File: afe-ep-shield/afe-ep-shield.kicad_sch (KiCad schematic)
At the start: 15 parts, among them J1 Conn_02x06_Odd_Even, J2 Conn_02x06_Odd_Even, J3 Conn_02x12_Odd_Even, J4 Conn_02x12_Odd_Even, J5 Conn_02x20_Odd_Even, U1 Dual_Buffer, U2 Dual_Buffer

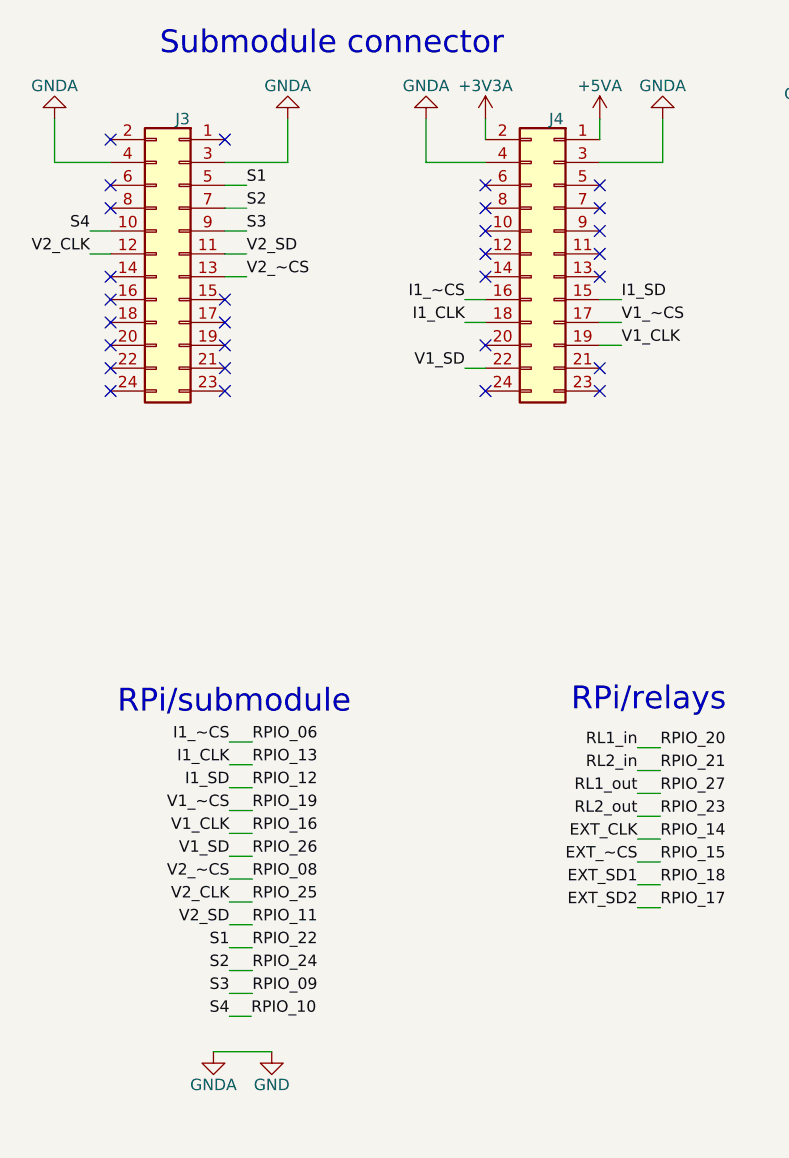
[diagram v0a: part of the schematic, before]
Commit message: Fixed afe shield connector
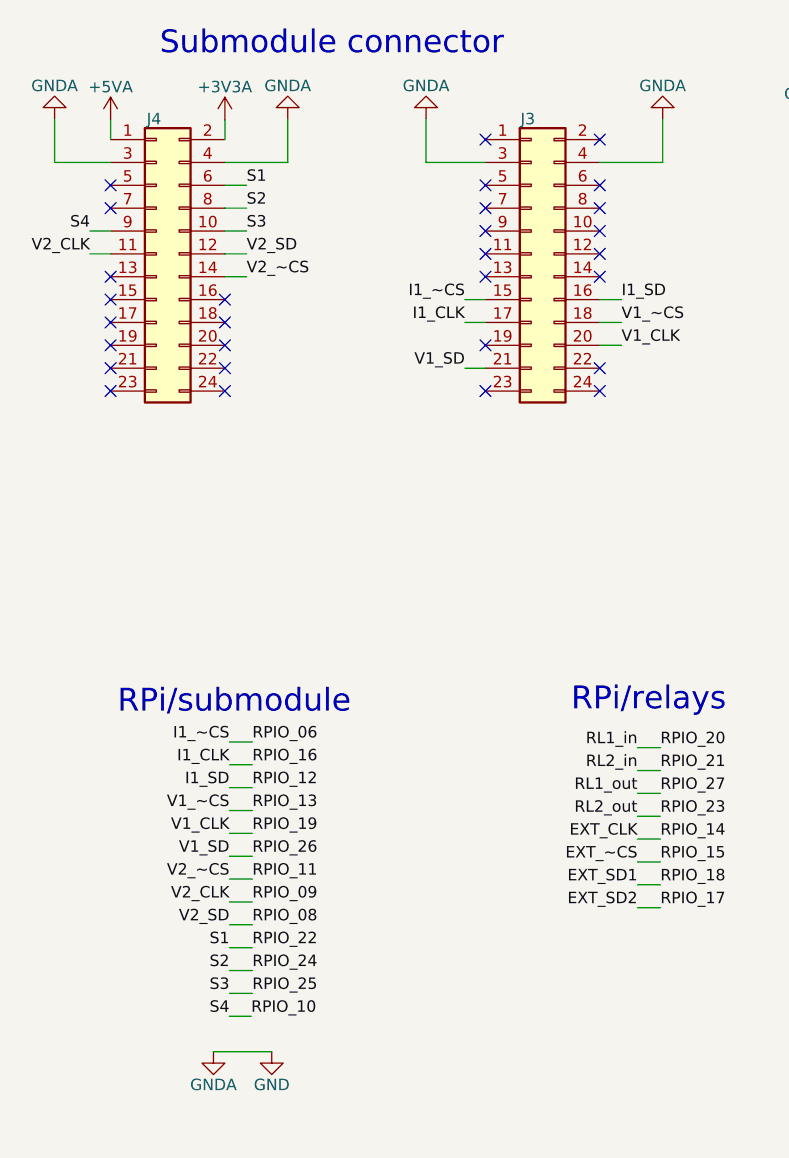
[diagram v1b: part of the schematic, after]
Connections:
- net I1_CLK: now also J3.17 (Pin_17), J5.36 (Pin_36); no longer J4.18 (Pin_18), J5.33 (Pin_33)
- net I1_SD: now also J3.16 (Pin_16); no longer J4.15 (Pin_15)
- net I1_~CS: now also J3.15 (Pin_15); no longer J4.16 (Pin_16)
- net RPIO_08: now also J4.12 (Pin_12); no longer J3.13 (Pin_13)
- net RPIO_09: now also J4.11 (Pin_11); no longer J3.9 (Pin_9)
- net RPIO_10: now also J4.9 (Pin_9); no longer J3.10 (Pin_10)
- net RPIO_11: now also J4.14 (Pin_14); no longer J3.11 (Pin_11)
- net RPIO_19: now also J3.20 (Pin_20); no longer J4.17 (Pin_17)
- net RPIO_22: now also J4.6 (Pin_6); no longer J3.5 (Pin_5)
- net RPIO_24: now also J4.8 (Pin_8); no longer J3.7 (Pin_7)
- net RPIO_25: now also J4.10 (Pin_10); no longer J3.12 (Pin_12)
- net RPIO_26: now also J3.21 (Pin_21); no longer J4.22 (Pin_22)
- net RPIO_13: now reaches J3.18 (Pin_18)
- net RPIO_13: now also J5.33 (Pin_33)
- net RPIO_16: no longer names the net of J4.19 (Pin_19)
- net RPIO_16: no longer J5.36 (Pin_36)
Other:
- moved on the sheet: J3, J4

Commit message: Connected 3V3A and 3V3 in afe shield
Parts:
- added R3: 0R, Resistor_SMD:R_0805_2012Metric, symbol Device:R_Small
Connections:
- net +3V3: now also J5.17 (Pin_17), R3.1; no longer J5.1 (Pin_1)
- net +3V3A: now also J3.2 (Pin_2), R3.2; no longer J4.2 (Pin_2)
- net GND: no longer J5.17 (Pin_17)
- no-connect marks 38 -> 39
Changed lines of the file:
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@@
   (junction (at 192.024 33.147) (diameter 0) (color 0 0 0 0)
-  )
-  (junction (at 98.552 48.768) (diameter 0) (color 0 0 0 0)
   )
   (junction (at 192.024 30.607) (diameter 0) (color 0 0 0 0)
@@
   (no_connect (at 170.307 30.607))
   (no_connect (at 63.373 27.559))
-  (no_connect (at 76.073 27.559))
+  (no_connect (at 34.417 27.559))
   (no_connect (at 109.601 30.988))
+  (no_connect (at 109.601 28.448))
   (no_connect (at 34.417 47.879))
   (no_connect (at 34.417 50.419))
@@
     (stroke (width 0) (type default) (color 0 0 0 0))
   )
+  (wire (pts (xy 57.785 62.23) (xy 57.785 64.77))
+    (stroke (width 0) (type default) (color 0 0 0 0))
+  )
   (wire (pts (xy 34.417 40.259) (xy 36.83 40.259))
     (stroke (width 0) (type default) (color 0 0 0 0))
@@
     (stroke (width 0) (type default) (color 0 0 0 0))
   )
+  (wire (pts (xy 50.165 64.77) (xy 47.625 64.77))
+    (stroke (width 0) (type default) (color 0 0 0 0))
+  )
   (wire (pts (xy 122.301 56.388) (xy 124.841 56.388))
     (stroke (width 0) (type default) (color 0 0 0 0))
@@
     (stroke (width 0) (type default) (color 0 0 0 0))
   )
-  (wire (pts (xy 34.417 25.4) (xy 34.417 27.559))
-    (stroke (width 0) (type default) (color 0 0 0 0))
-  )
   (wire (pts (xy 258.191 150.749) (xy 260.985 150.749))
     (stroke (width 0) (type default) (color 0 0 0 0))
@@
     (stroke (width 0) (type default) (color 0 0 0 0))
   )
-  (wire (pts (xy 98.552 48.768) (xy 109.601 48.768))
-    (stroke (width 0) (type default) (color 0 0 0 0))
-  )
   (wire (pts (xy 34.925 109.728) (xy 37.465 109.728))
     (stroke (width 0) (type default) (color 0 0 0 0))
@@
     (stroke (width 0) (type default) (color 0 0 0 0))
   )
-  (wire (pts (xy 98.552 48.768) (xy 98.552 38.608))
-    (stroke (width 0) (type default) (color 0 0 0 0))
-  )
   (wire (pts (xy 80.264 97.663) (xy 82.804 97.663))
     (stroke (width 0) (type default) (color 0 0 0 0))
@@
     (stroke (width 0) (type default) (color 0 0 0 0))
   )
+  (wire (pts (xy 93.472 48.768) (xy 109.601 48.768))
+    (stroke (width 0) (type default) (color 0 0 0 0))
+  )
   (wire (pts (xy 19.304 167.64) (xy 19.304 170.18))
     (stroke (width 0) (type default) (color 0 0 0 0))
@@
     (stroke (width 0) (type default) (color 0 0 0 0))
   )
-  (wire (pts (xy 98.552 48.768) (xy 98.552 58.928))
+  (wire (pts (xy 98.552 38.608) (xy 98.552 58.928))
     (stroke (width 0) (type default) (color 0 0 0 0))
   )
@@
     (stroke (width 0) (type default) (color 0 0 0 0))
   )
-  (wire (pts (xy 109.601 26.162) (xy 109.601 28.448))
-    (stroke (width 0) (type default) (color 0 0 0 0))
-  )
   (wire (pts (xy 34.925 119.888) (xy 37.465 119.888))
     (stroke (width 0) (type default) (color 0 0 0 0))
@@
     (stroke (width 0) (type default) (color 0 0 0 0))
   )
+  (wire (pts (xy 93.472 26.162) (xy 93.472 48.768))
+    (stroke (width 0) (type default) (color 0 0 0 0))
+  )
   (wire (pts (xy 122.301 28.448) (xy 122.301 30.988))
     (stroke (width 0) (type default) (color 0 0 0 0))
@@
     (stroke (width 0) (type default) (color 0 0 0 0))
   )
+  (wire (pts (xy 47.625 64.77) (xy 47.625 62.23))
+    (stroke (width 0) (type default) (color 0 0 0 0))
+  )
   (wire (pts (xy 172.212 55.499) (xy 172.212 52.959))
     (stroke (width 0) (type default) (color 0 0 0 0))
   )
+  (wire (pts (xy 76.073 25.273) (xy 76.073 27.559))
+    (stroke (width 0) (type default) (color 0 0 0 0))
+  )
   (wire (pts (xy 34.417 42.799) (xy 36.83 42.799))
+    (stroke (width 0) (type default) (color 0 0 0 0))
+  )
+  (wire (pts (xy 55.245 64.77) (xy 57.785 64.77))
     (stroke (width 0) (type default) (color 0 0 0 0))
   )
@@
     (pin "1")
   )
+  (symbol (lib_id "Device:R_Small") (at 52.705 64.77 270) (mirror x) (unit 1)
+    (in_bom yes) (on_board yes)
+    (property "Reference" "R3" (id 0) (at 51.435 68.326 90)
+      (effects (font (size 1.27 1.27)) (justify left))
+    )
+    (property "Value" "0R" (id 1) (at 51.435 66.548 90)
+      (effects (font (size 1.27 1.27)) (justify left))
+    )
+    (property "Footprint" "Resistor_SMD:R_0805_2012Metric" (id 2) (at 52.705 64.77 0)
+      (effects (font (size 1.27 1.27)) hide)
+    )
+    (property "Datasheet" "~" (id 3) (at 52.705 64.77 0)
+      (effects (font (size 1.27 1.27)) hide)
+    )
+    (pin "1")
+    (pin "2")
+  )
   (symbol (lib_id "power:VCC") (at 205.359 52.959 0) (unit 1)
     (in_bom yes) (on_board yes)
@@
     )
     (property "Datasheet" "" (id 3) (at 205.359 52.959 0)
+      (effects (font (size 1.27 1.27)) hide)
+    )
+    (pin "1")
+  )
+  (symbol (lib_id "CL_power:+3V3A") (at 47.625 62.23 0) (unit 1)
+    (in_bom yes) (on_board yes)
+    (property "Reference" "#PWR06" (id 0) (at 47.625 66.04 0)
+      (effects (font (size 1.27 1.27)) hide)
+    )
+    (property "Value" "+3V3A" (id 1) (at 47.625 58.547 0))
+    (property "Footprint" "" (id 2) (at 47.625 62.23 0)
+      (effects (font (size 1.27 1.27)) hide)
+    )
+    (property "Datasheet" "" (id 3) (at 47.625 62.23 0)
       (effects (font (size 1.27 1.27)) hide)
     )
@@
     (pin "1")
   )
-  (symbol (lib_id "power:+3V3") (at 109.601 26.162 0) (unit 1)
-    (in_bom yes) (on_board yes)
-    (property "Reference" "#PWR010" (id 0) (at 109.601 29.972 0)
-      (effects (font (size 1.27 1.27)) hide)
-    )
-    (property "Value" "+3V3" (id 1) (at 109.601 22.479 0))
-    (property "Footprint" "" (id 2) (at 109.601 26.162 0)
-      (effects (font (size 1.27 1.27)) hide)
-    )
-    (property "Datasheet" "" (id 3) (at 109.601 26.162 0)
+  (symbol (lib_id "power:+3V3") (at 93.472 26.162 0) (unit 1)
+    (in_bom yes) (on_board yes)
+    (property "Reference" "#PWR010" (id 0) (at 93.472 29.972 0)
+      (effects (font (size 1.27 1.27)) hide)
+    )
+    (property "Value" "+3V3" (id 1) (at 93.472 22.479 0))
+    (property "Footprint" "" (id 2) (at 93.472 26.162 0)
+      (effects (font (size 1.27 1.27)) hide)
+    )
+    (property "Datasheet" "" (id 3) (at 93.472 26.162 0)
       (effects (font (size 1.27 1.27)) hide)
     )
@@
     (pin "1")
   )
+  (symbol (lib_id "power:+3V3") (at 57.785 62.23 0) (unit 1)
+    (in_bom yes) (on_board yes)
+    (property "Reference" "#PWR018" (id 0) (at 57.785 66.04 0)
+      (effects (font (size 1.27 1.27)) hide)
+    )
+    (property "Value" "+3V3" (id 1) (at 57.785 58.547 0))
+    (property "Footprint" "" (id 2) (at 57.785 62.23 0)
+      (effects (font (size 1.27 1.27)) hide)
+    )
+    (property "Datasheet" "" (id 3) (at 57.785 62.23 0)
+      (effects (font (size 1.27 1.27)) hide)
+    )
+    (pin "1")
+  )
   (symbol (lib_id "power:+5VA") (at 195.199 52.959 0) (unit 1)
     (in_bom yes) (on_board yes)
@@
     )
     (property "Datasheet" "" (id 3) (at 195.199 52.959 0)
-      (effects (font (size 1.27 1.27)) hide)
-    )
-    (pin "1")
-  )
-  (symbol (lib_id "CL_power:+3V3A") (at 34.417 25.4 0) (unit 1)
-    (in_bom yes) (on_board yes)
-    (property "Reference" "#PWR06" (id 0) (at 34.417 29.21 0)
-      (effects (font (size 1.27 1.27)) hide)
-    )
-    (property "Value" "+3V3A" (id 1) (at 34.417 21.717 0))
-    (property "Footprint" "" (id 2) (at 34.417 25.4 0)
-      (effects (font (size 1.27 1.27)) hide)
-    )
-    (property "Datasheet" "" (id 3) (at 34.417 25.4 0)
       (effects (font (size 1.27 1.27)) hide)
     )
@@
     )
     (property "Datasheet" "~" (id 3) (at 50.927 170.18 0)
+      (effects (font (size 1.27 1.27)) hide)
+    )
+    (pin "1")
+  )
+  (symbol (lib_id "CL_power:+3V3A") (at 76.073 25.273 0) (unit 1)
+    (in_bom yes) (on_board yes)
+    (property "Reference" "#PWR03" (id 0) (at 76.073 29.083 0)
+      (effects (font (size 1.27 1.27)) hide)
+    )
+    (property "Value" "+3V3A" (id 1) (at 76.073 21.59 0))
+    (property "Footprint" "" (id 2) (at 76.073 25.273 0)
+      (effects (font (size 1.27 1.27)) hide)
+    )
+    (property "Datasheet" "" (id 3) (at 76.073 25.273 0)
       (effects (font (size 1.27 1.27)) hide)
     )
@@
       (reference "#PWR02") (unit 1) (value "GND2") (footprint "")
     )
+    (path "/c9ca5a02-4a92-4ede-8353-cdcee3bf0eab"
+      (reference "#PWR03") (unit 1) (value "+3V3A") (footprint "")
+    )
     (path "/5062f83d-89f0-4792-8e00-571ec97b672f"
       (reference "#PWR04") (unit 1) (value "GNDA") (footprint "")
@@
       (reference "#PWR05") (unit 1) (value "GNDA") (footprint "")
     )
-    (path "/ba33a77f-39d8-4c19-98c4-0781d5626147"
+    (path "/1eb827a1-4f15-4862-b424-9e4433aab4ab"
       (reference "#PWR06") (unit 1) (value "+3V3A") (footprint "")
     )
@@
       (reference "#PWR017") (unit 1) (value "GND") (footprint "")
     )
+    (path "/b9a37d45-115e-49e1-8875-034b1dac1c96"
+      (reference "#PWR018") (unit 1) (value "+3V3") (footprint "")
+    )
     (path "/616385eb-f160-45e7-8625-99c5ff23bcdb"
       (reference "#PWR020") (unit 1) (value "+5V") (footprint "")
@@
       (reference "R2") (unit 1) (value "0R") (footprint "Resistor_SMD:R_0805_2012Metric")
     )
+    (path "/186ecce9-2d54-4c54-bfff-532f0faaa069"
+      (reference "R3") (unit 1) (value "0R") (footprint "Resistor_SMD:R_0805_2012Metric")
+    )
     (path "/09186c4b-5b2e-43ec-bd76-f1d9e5804bab/246ee24e-c732-4642-900b-5064a6afce4a"

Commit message: Corrected relay connector and generated gerber files for afe shield
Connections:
- net RL1_in: now also J1.7 (Pin_7); no longer J1.11 (Pin_11)
- net RL1_out: now also J2.7 (Pin_7); no longer J2.11 (Pin_11)
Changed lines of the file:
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@@
   (junction (at 98.552 58.928) (diameter 0) (color 0 0 0 0)
   )
-  (no_connect (at 204.724 30.607))
   (no_connect (at 109.601 64.008))
   (no_connect (at 122.301 61.468))
@@
   (no_connect (at 21.717 47.879))
   (no_connect (at 21.717 42.799))
-  (no_connect (at 170.307 30.607))
+  (no_connect (at 170.307 25.527))
+  (no_connect (at 204.724 25.527))
   (no_connect (at 63.373 27.559))
   (no_connect (at 34.417 27.559))
@@
     (stroke (width 0) (type default) (color 0 0 0 0))
   )
-  (wire (pts (xy 204.724 25.527) (xy 207.645 25.527))
-    (stroke (width 0) (type default) (color 0 0 0 0))
-  )
   (wire (pts (xy 34.925 109.728) (xy 37.465 109.728))
     (stroke (width 0) (type default) (color 0 0 0 0))
@@
     (stroke (width 0) (type default) (color 0 0 0 0))
   )
+  (wire (pts (xy 170.307 30.607) (xy 173.228 30.607))
+    (stroke (width 0) (type default) (color 0 0 0 0))
+  )
   (wire (pts (xy 34.925 97.028) (xy 37.465 97.028))
     (stroke (width 0) (type default) (color 0 0 0 0))
@@
     (stroke (width 0) (type default) (color 0 0 0 0))
   )
-  (wire (pts (xy 170.307 25.527) (xy 173.228 25.527))
-    (stroke (width 0) (type default) (color 0 0 0 0))
-  )
   (wire (pts (xy 33.147 128.905) (xy 39.624 128.905))
     (stroke (width 0) (type default) (color 0 0 0 0))
   )
   (wire (pts (xy 157.607 35.687) (xy 157.607 38.227))
+    (stroke (width 0) (type default) (color 0 0 0 0))
+  )
+  (wire (pts (xy 204.724 30.607) (xy 207.645 30.607))
     (stroke (width 0) (type default) (color 0 0 0 0))
   )
@@
     (effects (font (size 1.27 1.27)) (justify right bottom))
   )
-  (label "RL1_out" (at 207.645 25.527 0)
+  (label "RL1_out" (at 207.645 30.607 0)
     (effects (font (size 1.27 1.27)) (justify left bottom))
   )
@@
     (effects (font (size 1.27 1.27)) (justify right bottom))
   )
-  (label "RL1_in" (at 173.228 25.527 0)
-    (effects (font (size 1.27 1.27)) (justify left bottom))
-  )
+  (label "RL1_in" (at 173.228 30.607 0)
+    (effects (font (size 1.27 1.27)) (justify left bottom))
+  )
